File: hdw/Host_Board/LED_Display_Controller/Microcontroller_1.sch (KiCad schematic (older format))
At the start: 1 part

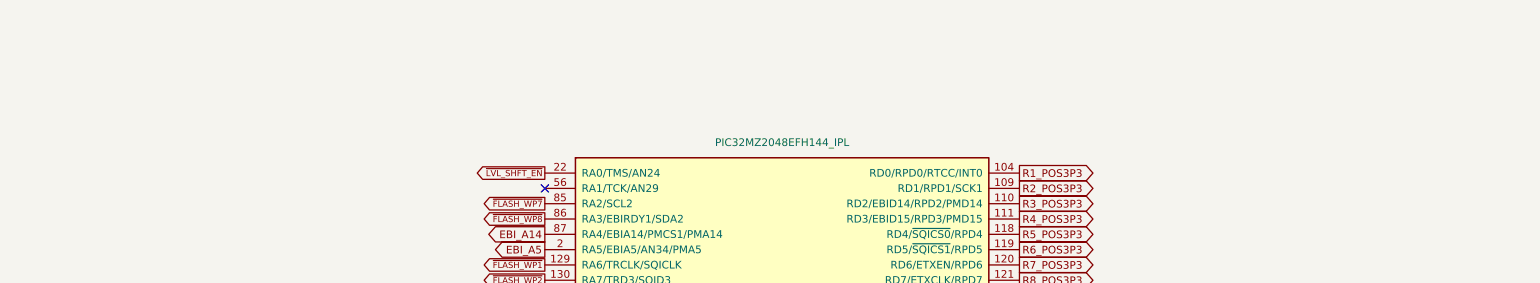
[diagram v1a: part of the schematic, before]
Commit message: Added titles and MU logo to each sheet
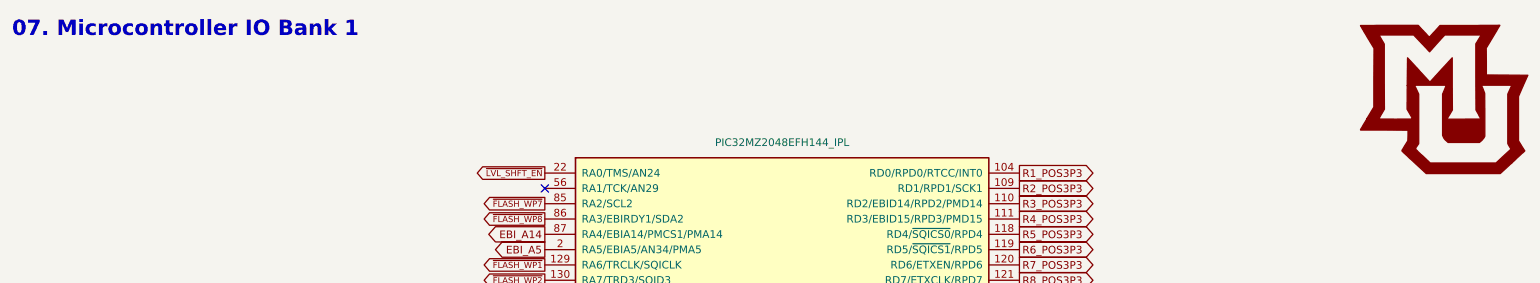
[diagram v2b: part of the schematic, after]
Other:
- note added: "07. Microcontroller IO Bank 1"
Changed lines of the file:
@@
 NoConn ~ 4030 5180
 NoConn ~ 4030 5480
+Text Notes 550  700  0    100  ~ 20
+07. Microcontroller IO Bank 1
+$Comp
+L LED_Display_Local_Library:MU_Logo #G?
+U 1 1 5BFF2F9C
+P 9900 1100
+F 0 "#G?" H 9900 614 60  0001 C CNN
+F 1 "MU_Logo" H 9900 1586 60  0001 C CNN
+F 2 "" H 9900 1100 50  0001 C CNN
+F 3 "" H 9900 1100 50  0001 C CNN
+	1    9900 1100
+	1    0    0    -1
+$EndComp
 $EndSCHEMATC
